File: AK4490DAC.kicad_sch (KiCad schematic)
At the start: 82 parts, among them IC1 LP5907MFX-3.3/NOPB, IC2 LP5907MFX-3.3/NOPB, IC3 LP5907MFX-3.3/NOPB, IC4 TPS7A2050PDBVR, IC5 MUSES8920, IC6 MUSES8920, IC7 MUSES8920, IC8 TPS7A2050PDBVR, IC9 AMS1117, J1 JST_XA_B02B-XASK-1, J2 USB_B_Micro, J3 SPDIF_IN, J4 LINE_OUT_L, J5 LINE_OUT_R, T1 DA103C, U1 SN74LS06NSR, U2 PCM2704CDBR, U3 TCM809TENB713, U4 TCM809TENB713, U5 AK4118, U6 AK4490, U7 MCWI03-12D15, Y1 11.2896MHz, Y2 12MHz

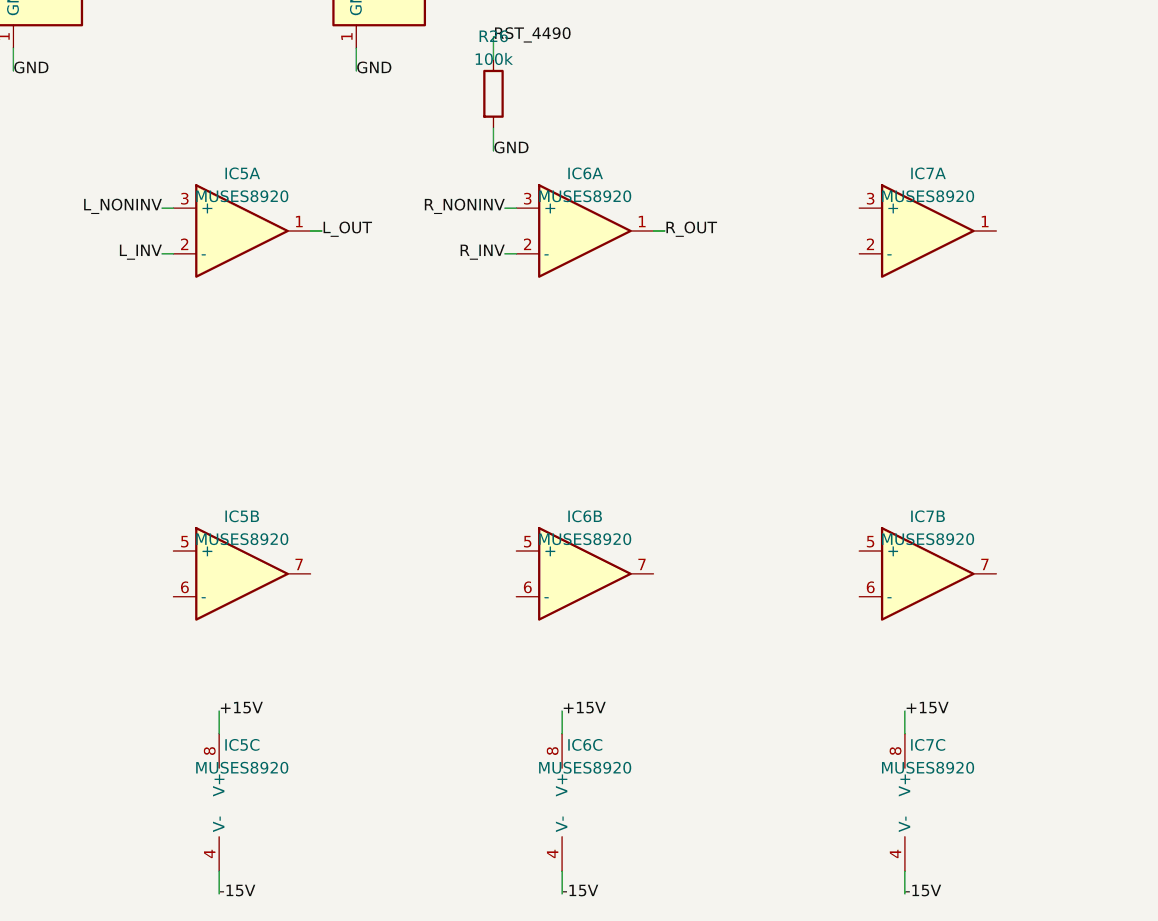
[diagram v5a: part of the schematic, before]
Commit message: Add MCWI03-12D15 footprint, remove spare IC7, terminate unused op-amp halves
- Created AK4490DAC.pretty/MCWI03-12D15.kicad_mod: custom SIP-8 THT
  footprint (single row, 2.54mm pitch, pin 4 physically absent, 21.8x9.3mm
  body per MCWI03 series datasheet mechanical outline). Pad size/drill are
  estimated (1.8mm/1.0mm) and noted as needing verification against the
  datasheet drawing before fab. Wired the Footprint property to
  "AK4490DAC:MCWI03-12D15" in the .kicad_sym master, the schematic's
  lib_symbols cache, and U7's placed instance.

- Removed IC7 (spare 3rd MUSES8920/TL072, all 3 units) entirely: it was
  placed and power-wired but never used for any signal. Also found and
  removed two dangling +15V/-15V power stub wires that had fed IC7's V+/V-
  pins - missed on the first pass because their stored coordinate
  (327.65999999999997) didn't textually match the "327.66" search string
  used to hunt for them (floating-point string representation trap).

- Terminated IC5-unit2 and IC6-unit2 (the unused op-amp half in each dual
  MUSES8920 package used for the L/R output stage) per standard unused-
  op-amp practice instead of leaving them floating: non-inverting input
  tied to GND, inverting input wired directly to the output (unity-gain
  follower), so each idle half sits at a defined 0V output instead of
  floating and risking oscillation/noise injection into the shared +-15V
  rail. IC5/IC6-unit3 (shared power pins) and unit1 (the actual signal
  path) are unchanged.

Incident during this work: a 3-point wire (pts (xy)(xy)(xy)) used for an
L-shaped feedback trace crashed kicad-cli's schematic parser (exit 3,
"回路図の読み込みに失敗しました") with no diagnostic detail. Root-caused via
bisection (reapplying each change from a clean HEAD checkout one at a time)
to KiCad's `wire` element only supporting 2-point segments, unlike
`polyline`. Fixed by splitting every L-shaped connection into two separate
2-point wire segments. Also caught and fixed a leftover debug placeholder
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
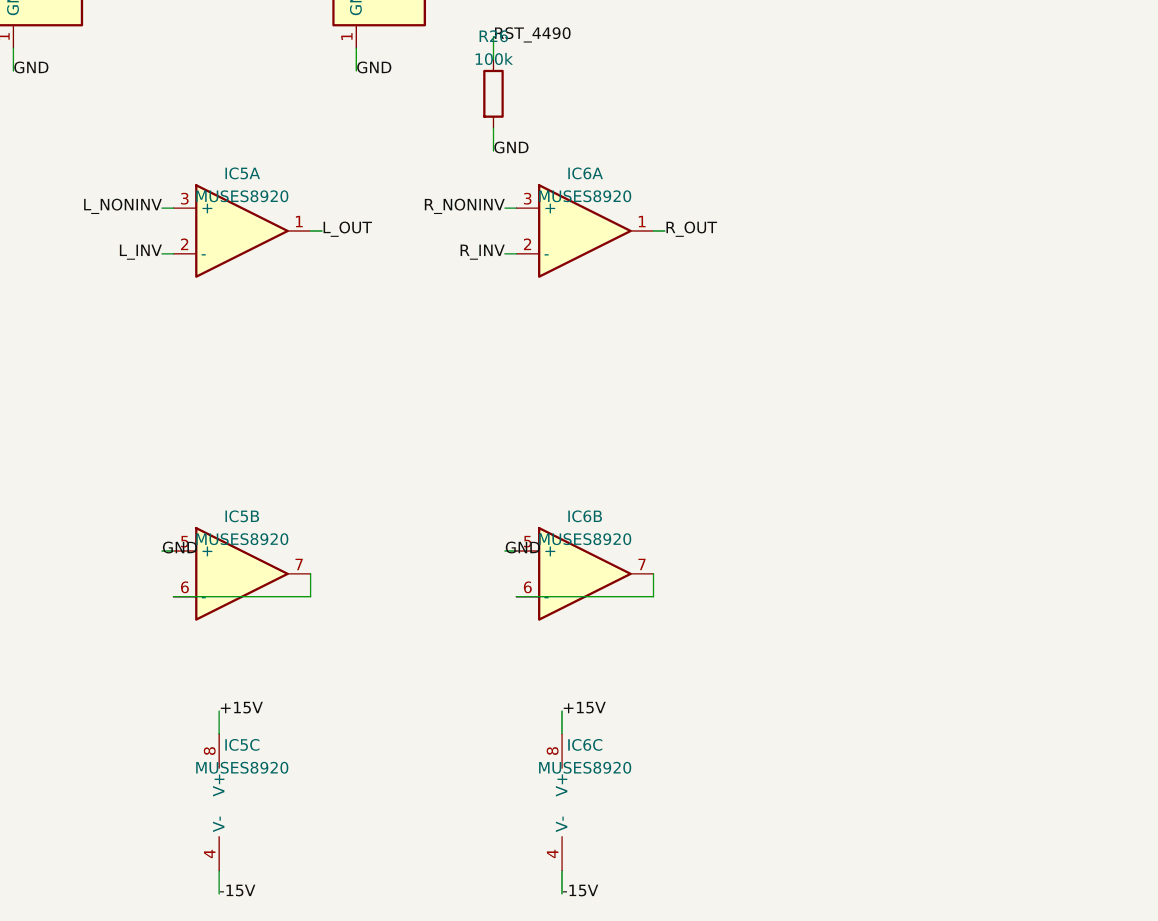
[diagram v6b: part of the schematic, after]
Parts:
- removed IC7: MUSES8920, Package_DIP:DIP-8_W7.62mm, symbol Amplifier_Operational:TL072
- U7: footprint (none) -> AK4490DAC:MCWI03-12D15
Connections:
- net GND: now also IC5.5 (+), IC6.5 (+)
- net at IC5.6 (-): now also IC5.7
- net at IC6.6 (-): now also IC6.7
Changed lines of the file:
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@@
 	)
 	(symbol
-		(lib_id "Amplifier_Operational:TL072")
-		(at 330.2 233.68 0)
-		(unit 1)
-		(exclude_from_sim no)
-		(in_bom yes)
-		(on_board yes)
-		(dnp no)
-		(property "Reference" "IC7"
-			(at 330.2 227.33 0)
-			(effects
-				(font
-					(size 1.27 1.27)
-				)
-			)
-		)
-		(property "Value" "MUSES8920"
-			(at 330.2 229.87 0)
-			(effects
-				(font
-					(size 1.27 1.27)
-				)
-			)
-		)
-		(property "Footprint" "Package_DIP:DIP-8_W7.62mm"
-			(at 330.2 233.68 0)
-			(effects
-				(font
-					(size 1.27 1.27)
-				)
-				(hide yes)
-			)
-		)
-		(property "Datasheet" ""
-			(at 330.2 233.68 0)
-			(effects
-				(font
-					(size 1.27 1.27)
-				)
-				(hide yes)
-			)
-		)
-		(property "Description" ""
-			(at 330.2 233.68 0)
-			(effects
-				(font
-					(size 1.27 1.27)
-				)
-			)
-		)
-		(pin "1"
-		)
-		(pin "2"
-		)
-		(pin "3"
-		)
-		(instances
-			(project "AK4490DAC"
-				(path "/43171a2d-7dc9-4067-85e7-263b74d7a8f4"
-					(reference "IC7")
-					(unit 1)
-				)
-			)
-		)
-	)
-	(symbol
 		(lib_id "74xx:74LS06N")
 		(at 381 25.4 0)
@@
 	)
 	(symbol
-		(lib_id "Amplifier_Operational:TL072")
-		(at 330.2 271.78000000000003 0)
-		(unit 2)
-		(exclude_from_sim no)
-		(in_bom yes)
-		(on_board yes)
-		(dnp no)
-		(property "Reference" "IC7"
-			(at 330.2 265.43 0)
-			(effects (font (size 1.27 1.27)))
-		)
-		(property "Value" "MUSES8920"
-			(at 330.2 267.97 0)
-			(effects (font (size 1.27 1.27)))
-		)
-		(property "Footprint" "Package_DIP:DIP-8_W7.62mm"
-			(at 330.2 271.78000000000003 0)
-			(effects (font (size 1.27 1.27)) hide)
-		)
-		(property "Datasheet" ""
-			(at 330.2 271.78000000000003 0)
-			(effects (font (size 1.27 1.27)) hide)
-		)
-		(property "Description" ""
-			(at 330.2 271.78000000000003 0)
-			(effects (font (size 1.27 1.27)) hide)
-		)
-		(pin "5"
-		)
-		(pin "6"
-		)
-		(pin "7"
-		)
-		(instances
-			(project "AK4490DAC"
-				(path "/43171a2d-7dc9-4067-85e7-263b74d7a8f4"
-					(reference "IC7")
-					(unit 2)
-				)
-			)
-		)
-	)
-	(symbol
-		(lib_id "Amplifier_Operational:TL072")
-		(at 330.2 297.18 0)
-		(unit 3)
-		(exclude_from_sim no)
-		(in_bom yes)
-		(on_board yes)
-		(dnp no)
-		(property "Reference" "IC7"
-			(at 330.2 290.83 0)
-			(effects (font (size 1.27 1.27)))
-		)
-		(property "Value" "MUSES8920"
-			(at 330.2 293.37 0)
-			(effects (font (size 1.27 1.27)))
-		)
-		(property "Footprint" "Package_DIP:DIP-8_W7.62mm"
-			(at 330.2 297.18 0)
-			(effects (font (size 1.27 1.27)) hide)
-		)
-		(property "Datasheet" ""
-			(at 330.2 297.18 0)
-			(effects (font (size 1.27 1.27)) hide)
-		)
-		(property "Description" ""
-			(at 330.2 297.18 0)
-			(effects (font (size 1.27 1.27)) hide)
-		)
-		(pin "8"
-		)
-		(pin "4"
-		)
-		(instances
-			(project "AK4490DAC"
-				(path "/43171a2d-7dc9-4067-85e7-263b74d7a8f4"
-					(reference "IC7")
-					(unit 3)
-				)
-			)
-		)
-	)
-	(symbol
 		(lib_id "AK4490DAC:MCWI03-12D15")
 		(at 389.89 260.35 0)
@@
 			(effects (font (size 1.27 1.27)))
 		)
-		(property "Footprint" ""
+		(property "Footprint" "AK4490DAC:MCWI03-12D15"
 			(at 389.89 260.35 0)
 			(effects (font (size 1.27 1.27)) hide)
@@
 			(effects (font (size 1.27 1.27)) hide)
 		)
-		(property "Description" "Isolated +-15V supply for output op-amp stage (IC5/IC6/IC7), fed from main DC input, reused from NEWDAC"
+		(property "Description" "Isolated +-15V supply for output op-amp stage (IC5/IC6), fed from main DC input, reused from NEWDAC"
 			(at 389.89 260.35 0)
 			(effects (font (size 1.27 1.27)) hide)
@@
 	(wire
 		(pts
-			(xy 327.65999999999997 289.56) (xy 327.65999999999997 287.02)
-		)
-		(stroke
-			(width 0)
-			(type default)
-		)
-	)
-	(label "+15V"
-		(at 327.65999999999997 287.02 0)
-		(effects
-			(font
-				(size 1.27 1.27)
-			)
-			(justify left)
-		)
-	)
-	(wire
-		(pts
-			(xy 327.65999999999997 304.8) (xy 327.65999999999997 307.34000000000003)
-		)
-		(stroke
-			(width 0)
-			(type default)
-		)
-	)
-	(label "-15V"
-		(at 327.65999999999997 307.34000000000003 0)
-		(effects
-			(font
-				(size 1.27 1.27)
-			)
-			(justify left)
-		)
-	)
-	(wire
-		(pts
 			(xy 13.97 101.6) (xy 11.43 101.6)
 		)
@@
 		)
 	)
+	(wire
+		(pts
+			(xy 246.38 269.24) (xy 245.11 269.24)
+		)
+		(stroke
+			(width 0)
+			(type default)
+		)
+	)
+	(label "GND"
+		(at 245.11 269.24 0)
+		(effects
+			(font
+				(size 1.27 1.27)
+			)
+			(justify left)
+		)
+	)
+	(wire
+		(pts
+			(xy 246.38 274.32) (xy 261.62 274.32)
+		)
+		(stroke
+			(width 0)
+			(type default)
+		)
+	)
+	(wire
+		(pts
+			(xy 261.62 274.32) (xy 261.62 271.78)
+		)
+		(stroke
+			(width 0)
+			(type default)
+		)
+	)
+	(wire
+		(pts
+			(xy 284.48 269.24) (xy 283.21 269.24)
+		)
+		(stroke
+			(width 0)
+			(type default)
+		)
+	)
+	(label "GND"
+		(at 283.21 269.24 0)
+		(effects
+			(font
+				(size 1.27 1.27)
+			)
+			(justify left)
+		)
+	)
+	(wire
+		(pts
+			(xy 284.48 274.32) (xy 299.72 274.32)
+		)
+		(stroke
+			(width 0)
+			(type default)
+		)
+	)
+	(wire
+		(pts
+			(xy 299.72 274.32) (xy 299.72 271.78)
+		)
+		(stroke
+			(width 0)
+			(type default)
+		)
+	)

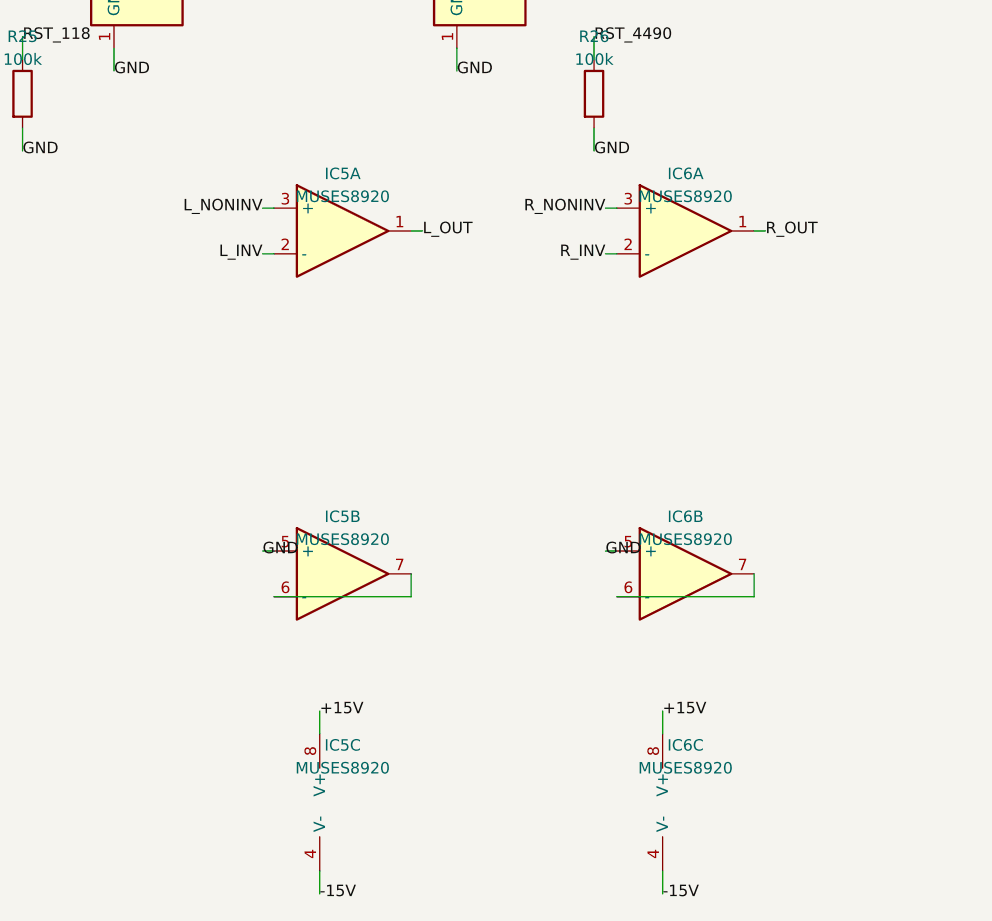
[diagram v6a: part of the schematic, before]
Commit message: Consolidate output op-amps: move R channel onto IC5, remove IC6
Per user request ("IC5,6は統合できないの？"): since each channel's
Fig.40 filter op-amp only used one half of its dual MUSES8920 package
(the other half was just terminated as a safety measure last commit),
consolidated both channels onto a single physical IC instead of two -
this is the standard approach for a stereo dual-op-amp stage and saves
one IC from the BOM.

- IC5-unit1 (L channel, unchanged) + IC5-unit2 (now carries R channel,
  previously just a grounded/follower-terminated spare half)
- Moved the R_NONINV/R_INV/R_OUT stub-wire+label connections from
  IC6-unit1's pins to the equivalent IC5-unit2 pins (5/6/7), reusing the
  same net label names so the existing Fig.40 R-channel resistor/cap
  network (R11-R21/R23, C22-C27, C32/C33) needed no changes.
- Removed IC6 entirely: unit1 (old R-channel signal pins), unit2 (the
  GND-tie/follower termination added last commit for the now-unnecessary
  spare half), and unit3 (+-15V power pins), including all their wiring.
- Updated U7 (MCWI03-12D15)'s Description to reflect IC5 alone (unit1=L,
  unit2=R) as the load instead of IC5/IC6.

Verified via kicad-cli sch erc: exit 0, 239 violations (down from 242),
same violation-category set as before (pin_not_connected 171,
power_pin_not_driven 40, pin_not_driven 21, lib_symbol_mismatch 4 [IC5
x3 units + U1/74LS06N x1, the known cosmetic mismatch, down from 7 now
that IC6's 3 units are gone], missing_power_pin 1, missing_input_pin 1,
missing_unit 1). No pin_to_pin/multiple_net_names or other new
categories - confirmed the R-channel net re-homing didn't introduce a
coordinate collision like the earlier Fig.40 wiring bug.

Co-Authored-By: Claude Sonnet 5 <noreply@anthropic.com>
Claude-Session: https://claude.ai/code/session_01UHxU1bYnUhoAmCyc4Koj96
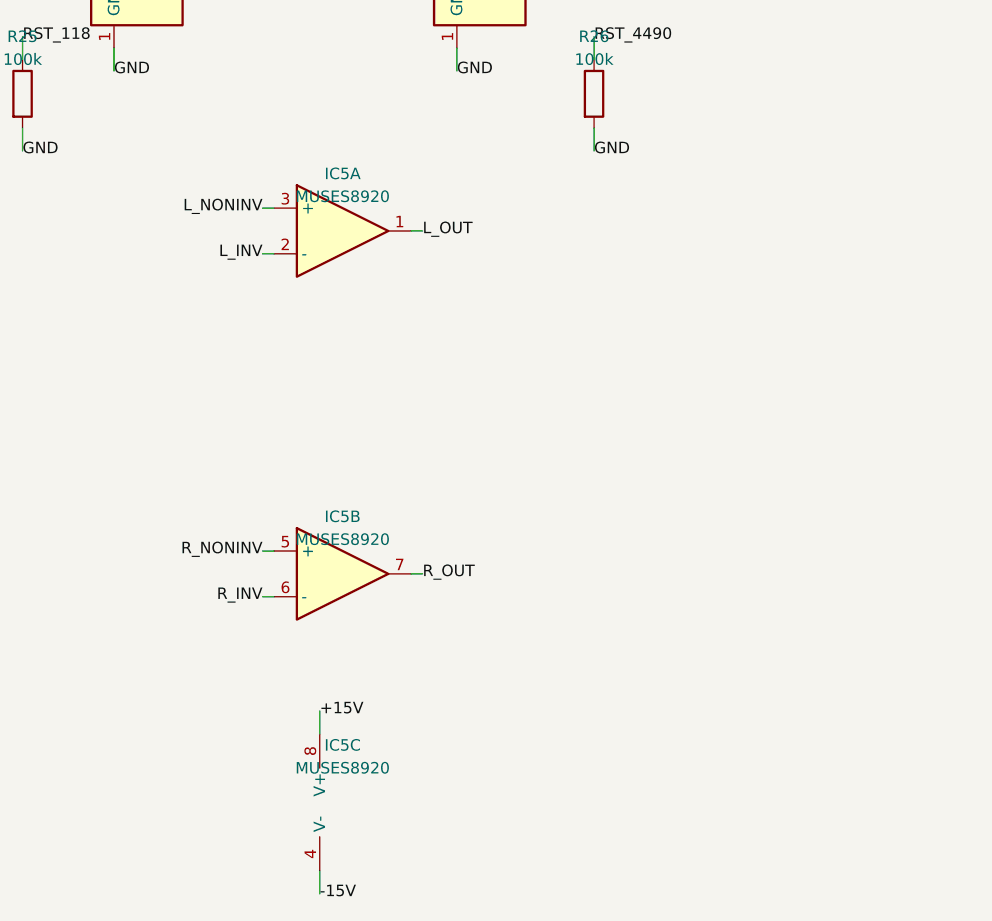
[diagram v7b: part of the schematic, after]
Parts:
- removed IC6: MUSES8920, Package_DIP:DIP-8_W7.62mm, symbol Amplifier_Operational:TL072
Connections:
- net GND: no longer IC5.5 (+)
- net R_INV: now also IC5.6 (-)
- net R_NONINV: now also IC5.5 (+)
- net R_OUT: now also IC5.7

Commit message: Decide SPDIF input as optical-only, switch USB to Type-C
Per user decisions ("光のみでいいかな" / "USBはCに変更"):

SPDIF input (J3): optical-only
- Replaced the generic 2-pin placeholder with an actual optical receiver:
  Toshiba TORX147(F,T), a 3-pin TOSLINK module (Output/GND/Vcc) chosen
  specifically because its Vcc range (2.7-3.6V, typ 3.0V) runs directly
  off the existing +3V3_118 rail - no new 5V rail needed, unlike the more
  common TORX173/5V family. New custom symbol + footprint (SIP-8 3-pin
  THT, body dims from the datasheet drawing; screw-mount hole not
  modeled, noted for follow-up).
- Rebuilt the RX0 front-end per AK4118 datasheet Fig.22 ("Consumer Input
  Circuit, Optical Input"): TORX147 Output -> 470R series R -> RX0, no
  AC-coupling cap. This replaces the previous Fig.21 (coax) network:
  R2 changed from 75R (coax termination) to 470R (optical series R,
  same physical part, repurposed), C4 changed from an 0.1uF AC-coupling
  cap to an 0.1uF Vcc decoupling cap for the new module - same value
  happened to already be correct for the new role.
- Wired AK4118's RX0 pin (previously completely unwired) with a "RX0"
  net label stub, matching the project's established stub+label style.

USB connector (J2): Micro-B -> Type-C
- Swapped Connector:USB_B_Micro for Connector:USB_C_Receptacle_USB2.0_16P
  (pinout matches the popular GCT USB4085 THT footprint used as the PCB
  footprint). USB2.0-only: D+/D- and VBUS wired (multi-pin groups tied
  via shared net labels), SBU1/SBU2 left NC (alt-mode, unused).
- Added R27/R28 (5.1k), pulling CC1/CC2 down to USB_GND - required by
  the USB Type-C spec for the port to be recognized as a UFP/device and
  enable VBUS; a bare USB-C receptacle does not work without these.
  GND/Shield tied to the isolated USB_GND domain per the connector's
  pre-existing description (matches original design intent, not yet a
  fully realized isolation barrier - PCM2704C-side wiring is unchanged/
  still deferred).

Incident caught before commit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
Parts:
- removed J2: USB_B_Micro, Connector_USB:USB_Micro-B_Molex-105017-0001, symbol Connector:USB_B_Micro
- added J2: USB_C_Receptacle_USB2.0_16P, Connector_USB:USB_C_Receptacle_GCT_USB4085, symbol Connector:USB_C_Receptacle_USB2.0_16P
- added R27, R28: 5.1k, Resistor_SMD:R_0603_1608Metric, symbol Device:R
- J3: value SPDIF_IN -> TORX147FT; footprint (none) -> AK4490DAC:TORX147FT; symbol Connector_Generic:Conn_01x02 -> AK4490DAC:TORX147FT
- R2: value 75 -> 470
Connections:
- net +3V3_118: now also C4.1, J3.3 (Vcc)
- net GND: now also C4.2, J3.2 (GND)
- net RX0: now reaches U5.42 (RX0)
- net RX0: now also R2.2
- net SPDIF_OPT: now reaches J3.1 (Output)
- net SPDIF_OPT: now also R2.1
- new net USB_CC1: J2.A5 (CC1), R27.1
- new net USB_CC2: J2.B5 (CC2), R28.1
- new net USB_D+: J2.A6 (D+), J2.B6 (D+)
- new net USB_D-: J2.A7 (D-), J2.B7 (D-)
- new net USB_GND: J2.A1 (GND), J2.A12 (GND), J2.B1 (GND), J2.B12 (GND), J2.S1 (SHIELD), R27.2, R28.2
- new net VBUS: J2.A4 (VBUS), J2.A9 (VBUS), J2.B4 (VBUS), J2.B9 (VBUS)
